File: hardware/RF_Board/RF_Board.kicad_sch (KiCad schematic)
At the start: 129 parts, among them J1 Conn_Coaxial, J2 Conn_01x04_Male, J3 Conn_Coaxial, J4 Conn_01x04_Male, J5 Conn_01x06_Female, J6 Conn_01x06_Female, J7 Conn_01x06_Female, J8 L77TSAH15SOL2RM8, J9 Conn_01x09_Male, Q1 2N7002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

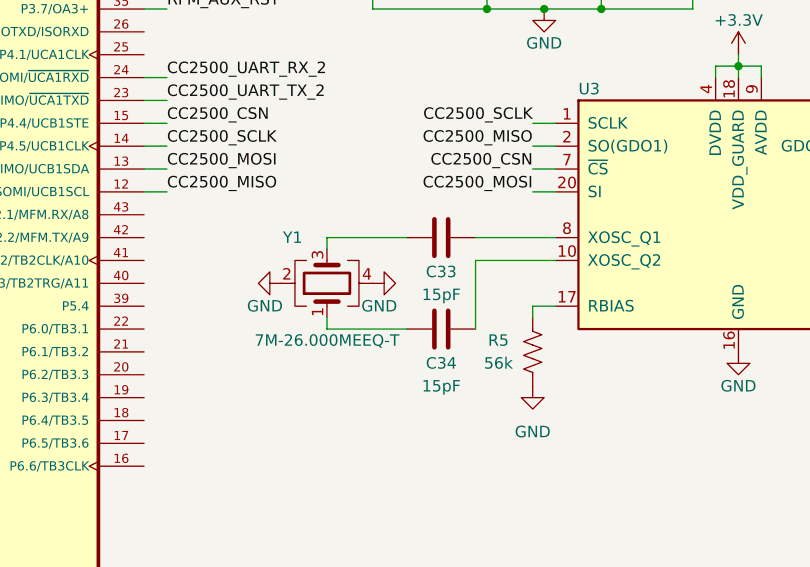
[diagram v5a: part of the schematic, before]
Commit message: add fixed Rev. 2 RF PCB
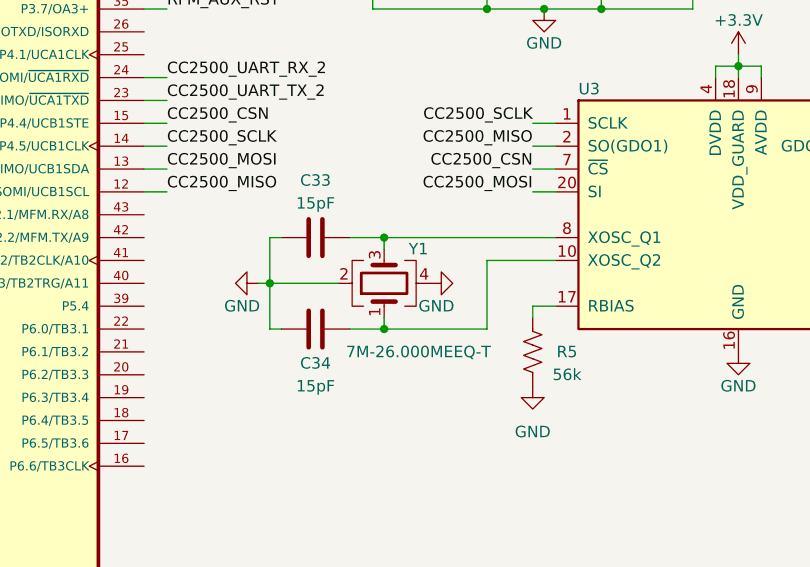
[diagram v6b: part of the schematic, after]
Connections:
- net GND: now also C33.1, C34.1
- net at C34.2, U3.10 (XOSC_Q2): now also Y1.1
- net at C33.2, U3.8 (XOSC_Q1): now also Y1.3
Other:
- moved on the sheet: C33, C34, Y1
